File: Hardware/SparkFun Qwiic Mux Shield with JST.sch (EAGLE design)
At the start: 63 parts, among them U1 ARDUINO UNO, U2 TCA9548A

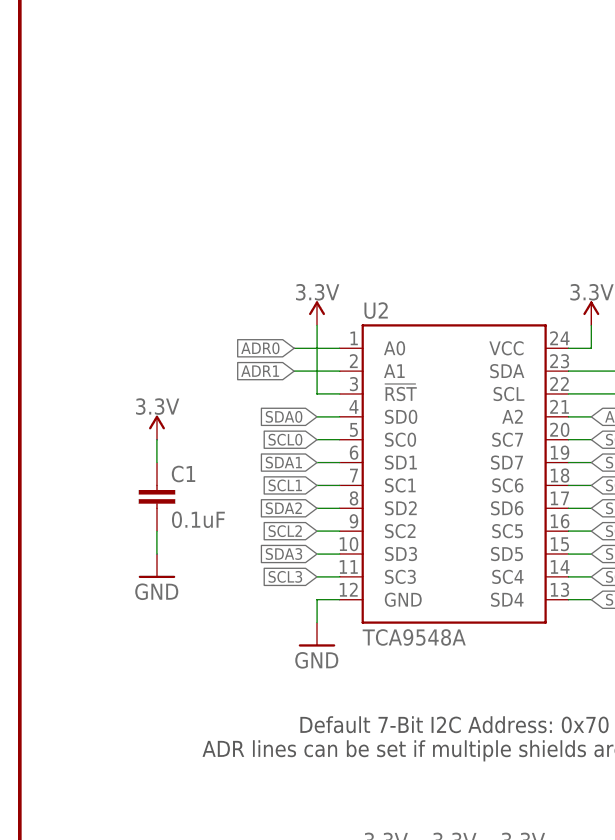
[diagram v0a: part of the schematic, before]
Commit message: Breaking out reset pin
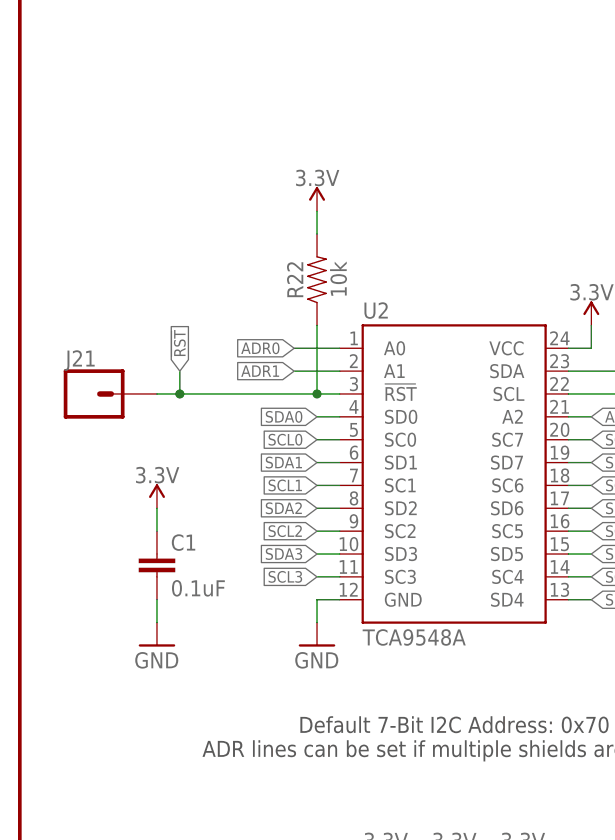
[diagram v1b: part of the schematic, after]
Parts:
- added J21: (no value), SparkFun-Connectors:CONN_01
- added R22: 10k, SparkFun-Resistors:10KOHM-0603-1/10W-1%
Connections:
- new net !RST: J21.1, R22.1, U2.!RST
- net 3.3V: now also R22.2; no longer U2.!RST
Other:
- moved on the sheet: C1
